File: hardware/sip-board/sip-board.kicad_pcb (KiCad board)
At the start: 8 copper layers, 17 x 50 mm, 85 parts, among them IC1 XC7S15-1CPGA196C, J1 Conn_01x06_Pin, J2 Conn_01x10_Pin, J3 Conn_01x10_Pin, J4 Conn_01x10_Pin, J5 Conn_01x10_Pin, SW1 SW_DIP_x03, SW2 SW_RESET, U1 TLV75718PDRV, U2 TLV75733PDRV, U3 TLV75710PDRV, U4 M95256-WMN6P

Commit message: follow marco stackup
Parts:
- removed C1, C11: 10u, Capacitor_SMD:C_0201_0603Metric
- removed C10, C12, C13, C20, C21, C22, C23, C28, C30, C31, C32, C33, C34, C7, C8, C9: 0.47u, Capacitor_SMD:C_0201_0603Metric
- removed C14, C15, C25, C35, C5: 100u, Capacitor_SMD:C_0201_0603Metric
- removed C16, C17, C18, C19, C26, C27, C29, C36, C37: 4.7u, Capacitor_SMD:C_0201_0603Metric
- removed C2, C3: 50u, Capacitor_SMD:C_0201_0603Metric
- removed C24: 47u, Capacitor_SMD:C_0201_0603Metric
- removed C4, C6: 1u, Capacitor_SMD:C_0201_0603Metric
- removed D1: D_Small, Diode_SMD:D_0201_0603Metric
- removed D2, D3, D4, D5, D6: LED, LED_SMD:LED_0201_0603Metric
- removed IC1: XC7S15-1CPGA196C, fpga_stuff:BGA196C50P14X14_800X800X110
- removed J1: Conn_01x06_Pin, Connector_PinHeader_2.54mm:PinHeader_1x06_P2.54mm_Vertical_SMD_Pin1Right
- removed R1, R2, R3: 1k, Resistor_SMD:R_0201_0603Metric
- removed R10, R11, R12, R13, R4, R5, R6, R7, R8, R9: 10k, Resistor_SMD:R_0201_0603Metric
- removed R14: 5k, Resistor_SMD:R_0201_0603Metric
- removed R15: 2k4, Resistor_SMD:R_0201_0603Metric
- removed R16: 4k7, Resistor_SMD:R_0201_0603Metric
- removed R17, R20: 5k7, Resistor_SMD:R_0201_0603Metric
- removed R18: 2k3, Resistor_SMD:R_0201_0603Metric
- removed R19: 3k, Resistor_SMD:R_0201_0603Metric
- removed SW1: SW_DIP_x03, Button_Switch_SMD:SW_DIP_SPSTx03_Slide_6.7x9.18mm_W6.73mm_P2.54mm_LowProfile_JPin
- removed SW2: SW_RESET, Button_Switch_SMD:SW_Push_1P1T_NO_6x6mm_H9.5mm
- removed U1: TLV75718PDRV, Package_SON:WSON-6-1EP_2x2mm_P0.65mm_EP1x1.6mm
- removed U10, U11, U12, U13, U14, U5, U6, U7, U8, U9: ~, hardware:NXB0104_XQFN12
- removed U2: TLV75733PDRV, Package_SON:WSON-6-1EP_2x2mm_P0.65mm_EP1x1.6mm
- removed U3: TLV75710PDRV, Package_SON:WSON-6-1EP_2x2mm_P0.65mm_EP1x1.6mm
- removed U4: M95256-WMN6P, Package_SO:SOIC-8_3.9x4.9mm_P1.27mm
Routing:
- net +5V: track 132.3 -> 0.00 mm, vias 12 -> 0
- net MOSI: track 65.3 -> 0.00 mm, vias 6 -> 0
- net +3V3: track 64.7 -> 0.00 mm, vias 41 -> 0
- net GND: track 58.4 -> 0.00 mm, vias 58 -> 0
- net CS: track 46.4 -> 0.00 mm, vias 3 -> 0
- net CCLK: track 23.3 -> 0.00 mm, vias 3 -> 0
- net TDO: track 20.8 -> 0.00 mm, vias 3 -> 0
- net +1V8: track 15.1 -> 0.00 mm, vias 4 -> 0
- net M2_CONFIG: track 13.7 -> 0.00 mm, vias 2 -> 0
- net M1_CONFIG: track 13.0 -> 0.00 mm, vias 2 -> 0
- net M0_CONFIG: track 12.7 -> 0.00 mm, vias 2 -> 0
- net PROGRAM_B: track 11.2 -> 0.00 mm
- net DIN: track 11.0 -> 0.00 mm, vias 2 -> 0
- net +1V0: track 10.5 -> 0.00 mm, vias 13 -> 0
- net Net-(C11-Pad1): track 9.44 -> 0.00 mm
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- added copper zone on In6.Cu, net GND
- removed copper zone on In3.Cu, net +1V0
- removed copper zone on In2.Cu, net +3V3
- removed copper zone on B.Cu, net GND
- removed copper zone on In4.Cu, net GND
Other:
- board text removed: "+5V"
- board text removed: "1V0"
- board text removed: "1V8"
- board text removed: "3V3"
- board text removed: "A0"
- board text removed: "A1"
- board text removed: "A10"
- board text removed: "A11"
- board text removed: "A12"
- board text removed: "A13"
- board text removed: "A14"
- board text removed: "A15"
- board text removed: "A2"
- board text removed: "A3"
- board text removed: "A4"
- board text removed: "A5"
- board text removed: "A6"
- board text removed: "A7"
- board text removed: "A8"
- board text removed: "A9"
- board text removed: "BUSAK"
- board text removed: "BUSRQ"
- board text removed: "CLK"
- board text removed: "D0"
- board text removed: "D1"
- board text removed: "D2"
- board text removed: "D3"
- board text removed: "D4"
- board text removed: "D5"
- board text removed: "D6"
- board text removed: "D7"
- board text removed: "GND"
- board text removed: "HALT"
- board text removed: "INT"
- board text removed: "IORQ"
- board text removed: "M0"
- board text removed: "M1"
- board text removed: "M2"
- board text removed: "MREQ"
- board text removed: "NMI"
- board text removed: "RD"
- board text removed: "RESET"
- board text removed: "RFSH"
- board text removed: "SPI - [001] JTAG - [101]"
- board text removed: "SPI PROM"
- board text removed: "VDD GND CCLK TDO MOSI CS"
- board text removed: "WAIT"
- board text removed: "WR"
- board text removed: "Z80 Drop In Connor Leu UT Austin '25"
- board text removed: "off/on"

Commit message: wip layout, part placement
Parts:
- added C1: 10u, Capacitor_SMD:C_0201_0603Metric, F.Cu at (141.7, 94.3)
- added C10: 0.47u, Capacitor_SMD:C_0201_0603Metric, B.Cu at (147.2, 105.8)
- added C11: 10u, Capacitor_SMD:C_0201_0603Metric, F.Cu at (150.9, 116.4)
- added C12: 0.47u, Capacitor_SMD:C_0201_0603Metric, B.Cu at (144.0, 102.2)
- added C13: 0.47u, Capacitor_SMD:C_0201_0603Metric, B.Cu at (147.2, 106.7)
- added C14: 100u, Capacitor_SMD:C_0201_0603Metric, F.Cu at (141.8, 108.8)
- added C15: 100u, Capacitor_SMD:C_0201_0603Metric, F.Cu at (144.9, 108.9)
- added C16: 4.7u, Capacitor_SMD:C_0201_0603Metric, F.Cu at (101.4, 62.9)
- added C17: 4.7u, Capacitor_SMD:C_0201_0603Metric, F.Cu at (147.9, 108.8)
- added C18: 4.7u, Capacitor_SMD:C_0201_0603Metric, F.Cu at (149.8, 108.8)
- added C19: 4.7u, Capacitor_SMD:C_0201_0603Metric, F.Cu at (148.9, 108.8)
- added C2: 50u, Capacitor_SMD:C_0201_0603Metric, F.Cu at (145.6, 94.3)
- added C20: 0.47u, Capacitor_SMD:C_0201_0603Metric, B.Cu at (145.6, 103.8)
- added C21: 0.47u, Capacitor_SMD:C_0201_0603Metric, B.Cu at (144.0, 103.8)
- added C22: 0.47u, Capacitor_SMD:C_0201_0603Metric, B.Cu at (143.6, 103.0)
- added C23: 0.47u, Capacitor_SMD:C_0201_0603Metric, B.Cu at (144.0, 104.6)
- added C24: 47u, Capacitor_SMD:C_0201_0603Metric, F.Cu at (142.9, 108.8)
- added C25: 100u, Capacitor_SMD:C_0201_0603Metric, F.Cu at (145.9, 108.9)
- added C26: 4.7u, Capacitor_SMD:C_0201_0603Metric, F.Cu at (143.9, 108.8)
- added C27: 4.7u, Capacitor_SMD:C_0201_0603Metric, F.Cu at (150.7, 107.0)
- added C28: 0.47u, Capacitor_SMD:C_0201_0603Metric, B.Cu at (146.2, 101.3)
- added C29: 4.7u, Capacitor_SMD:C_0201_0603Metric, F.Cu at (150.7, 105.9)
- added C3: 50u, Capacitor_SMD:C_0201_0603Metric, F.Cu at (149.3, 94.3)
- added C30: 0.47u, Capacitor_SMD:C_0201_0603Metric, B.Cu at (146.2, 102.2)
- added C31: 0.47u, Capacitor_SMD:C_0201_0603Metric, B.Cu at (144.2, 105.8)
- added C32: 0.47u, Capacitor_SMD:C_0201_0603Metric, B.Cu at (144.1, 106.7)
- added C33: 0.47u, Capacitor_SMD:C_0201_0603Metric, F.Cu at (140.5, 107.0)
- added C34: 0.47u, Capacitor_SMD:C_0201_0603Metric, F.Cu at (140.5, 106.0)
- added C35: 100u, Capacitor_SMD:C_0201_0603Metric, F.Cu at (146.9, 108.9)
- added C36: 4.7u, Capacitor_SMD:C_0201_0603Metric, F.Cu at (150.7, 104.8)
- added C37: 4.7u, Capacitor_SMD:C_0201_0603Metric, F.Cu at (150.7, 103.6)
- added C4: 1u, Capacitor_SMD:C_0201_0603Metric, F.Cu at (146.2, 98.3)
- added C5: 100u, Capacitor_SMD:C_0201_0603Metric, F.Cu at (149.9, 98.3)
- added C6: 1u, Capacitor_SMD:C_0201_0603Metric, F.Cu at (142.3, 98.3)
- added C7: 0.47u, Capacitor_SMD:C_0201_0603Metric, B.Cu at (145.7, 106.7)
- added C8: 0.47u, Capacitor_SMD:C_0201_0603Metric, B.Cu at (145.7, 105.8)
- added C9: 0.47u, Capacitor_SMD:C_0201_0603Metric, B.Cu at (144.0, 101.3)
- added CFG1: SW_DIP_x03, Button_Switch_SMD:SW_DIP_SPSTx03_Slide_6.7x9.18mm_W6.73mm_P2.54mm_LowProfile_JPin, F.Cu at (145.4, 123.5)
- added D1: D_Small, Diode_SMD:D_0201_0603Metric, F.Cu at (151.8, 85.7)
- added D3: LED, LED_SMD:LED_0201_0603Metric, F.Cu at (139.9, 97.1)
- added D4: LED, LED_SMD:LED_0201_0603Metric, F.Cu at (143.8, 97.1)
- added D5: LED, LED_SMD:LED_0201_0603Metric, F.Cu at (147.5, 97.1)
- added DONE1: LED, LED_SMD:LED_0201_0603Metric, F.Cu at (145.7, 110.6)
- added IC1: XC7S15-1CPGA196C, fpga_stuff:BGA196C50P14X14_800X800X110, F.Cu at (145.6, 103.3)
- added INIT1: LED, LED_SMD:LED_0201_0603Metric, F.Cu at (142.6, 110.7)
- added J1: Conn_01x06_Pin, Connector_PinHeader_2.54mm:PinHeader_1x06_P2.54mm_Vertical_SMD_Pin1Left, F.Cu at (145.6, 83.3)
- added R1: 1k, Resistor_SMD:R_0201_0603Metric, F.Cu at (149.0, 118.3)
- added R10: 10k, Resistor_SMD:R_0201_0603Metric, F.Cu at (108.8, 64.6)
- added R11: 10k, Resistor_SMD:R_0201_0603Metric, F.Cu at (108.8, 66.4)
- added R12: 10k, Resistor_SMD:R_0201_0603Metric, F.Cu at (108.8, 68.1)
- added R13: 10k, Resistor_SMD:R_0201_0603Metric, F.Cu at (108.8, 69.9)
- added R14: 5k, Resistor_SMD:R_0201_0603Metric, F.Cu at (149.2, 110.7)
- added R15: 2k4, Resistor_SMD:R_0201_0603Metric, F.Cu at (111.2, 55.9)
- added R16: 4k7, Resistor_SMD:R_0201_0603Metric, F.Cu at (144.1, 110.7)
- added R17: 5k7, Resistor_SMD:R_0201_0603Metric, F.Cu at (147.2, 110.6)
- added R18: 2k3, Resistor_SMD:R_0201_0603Metric, F.Cu at (140.7, 98.3)
- added R19: 3k, Resistor_SMD:R_0201_0603Metric, F.Cu at (144.6, 98.3)
- added R2: 1k, Resistor_SMD:R_0201_0603Metric, F.Cu at (146.2, 118.3)
- added R20: 5k7, Resistor_SMD:R_0201_0603Metric, F.Cu at (148.3, 98.3)
- added R3: 1k, Resistor_SMD:R_0201_0603Metric, F.Cu at (143.6, 118.3)
- added R4: 10k, Resistor_SMD:R_0201_0603Metric, F.Cu at (108.8, 54.1)
- added R5: 10k, Resistor_SMD:R_0201_0603Metric, F.Cu at (108.8, 55.9)
- added R6: 10k, Resistor_SMD:R_0201_0603Metric, F.Cu at (108.8, 57.6)
- added R7: 10k, Resistor_SMD:R_0201_0603Metric, F.Cu at (108.8, 59.4)
- added R8: 10k, Resistor_SMD:R_0201_0603Metric, F.Cu at (108.8, 61.1)
- added R9: 10k, Resistor_SMD:R_0201_0603Metric, F.Cu at (108.8, 62.9)
- added SPIPROM1: M95256-WMN6P, Package_SO:SOIC-8_3.9x4.9mm_P1.27mm, F.Cu at (145.4, 89.6)
- added SW2: SW_RESET, Button_Switch_SMD:SW_Push_1P1T_NO_6x6mm_H9.5mm, F.Cu at (145.5, 114.5)
- added U1: TLV75718PDRV, Package_SON:WSON-6-1EP_2x2mm_P0.65mm_EP1x1.6mm, F.Cu at (145.6, 96.5)
- added U10: ~, hardware:NXB0104_XQFN12, F.Cu at (99.7, 52.5)
- added U11: ~, hardware:NXB0104_XQFN12, F.Cu at (102.8, 52.5)
- added U12: ~, hardware:NXB0104_XQFN12, F.Cu at (105.9, 52.5)
- added U13: ~, hardware:NXB0104_XQFN12, F.Cu at (109.0, 52.5)
- added U14: ~, hardware:NXB0104_XQFN12, F.Cu at (112.0, 52.5)
- added U2: TLV75733PDRV, Package_SON:WSON-6-1EP_2x2mm_P0.65mm_EP1x1.6mm, F.Cu at (149.3, 96.5)
- added U3: TLV75710PDRV, Package_SON:WSON-6-1EP_2x2mm_P0.65mm_EP1x1.6mm, F.Cu at (141.7, 96.5)
- added U5: ~, hardware:NXB0104_XQFN12, F.Cu at (131.9, 81.5)
- added U6: ~, hardware:NXB0104_XQFN12, F.Cu at (102.8, 48.5)
- added U7: ~, hardware:NXB0104_XQFN12, F.Cu at (105.9, 48.5)
- added U8: ~, hardware:NXB0104_XQFN12, F.Cu at (109.0, 48.5)
- added U9: ~, hardware:NXB0104_XQFN12, F.Cu at (112.0, 48.5)
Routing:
- net GND: track 0.00 -> 59.5 mm, vias 0 -> 67
- net +3V3: track 0.00 -> 35.1 mm, vias 0 -> 16
- net +5V: track 0.00 -> 29.4 mm
- net CS: track 0.00 -> 21.7 mm
- net +1V8: track 0.00 -> 12.5 mm, vias 0 -> 5
- net CCLK: track 0.00 -> 10.4 mm, vias 0 -> 2
- net +1V0: track 0.00 -> 9.76 mm, vias 0 -> 11
- net PROGRAM_B: track 0.00 -> 9.46 mm
- net Net-(C11-Pad1): track 0.00 -> 9.41 mm
- net MOSI: track 0.00 -> 6.57 mm, vias 0 -> 2
- net DONE: track 0.00 -> 5.55 mm, vias 0 -> 2
- net Net-(IC1-INIT_B_0): track 0.00 -> 4.91 mm, vias 0 -> 2
- net VDD: track 0.00 -> 3.86 mm
- net Net-(D4-A): track 0.00 -> 1.12 mm
- net Net-(D5-A): track 0.00 -> 1.08 mm
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- added copper zone on In4.Cu, net +1V0
- added copper zone on In3.Cu, net +3V3
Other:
- board text added: "CCLK"
- board text added: "CS"
- board text added: "File off bottom of THT connectors"
- board text added: "GND"
- board text added: "MOSI"
- board text added: "TDO"
- board text added: "VDD"

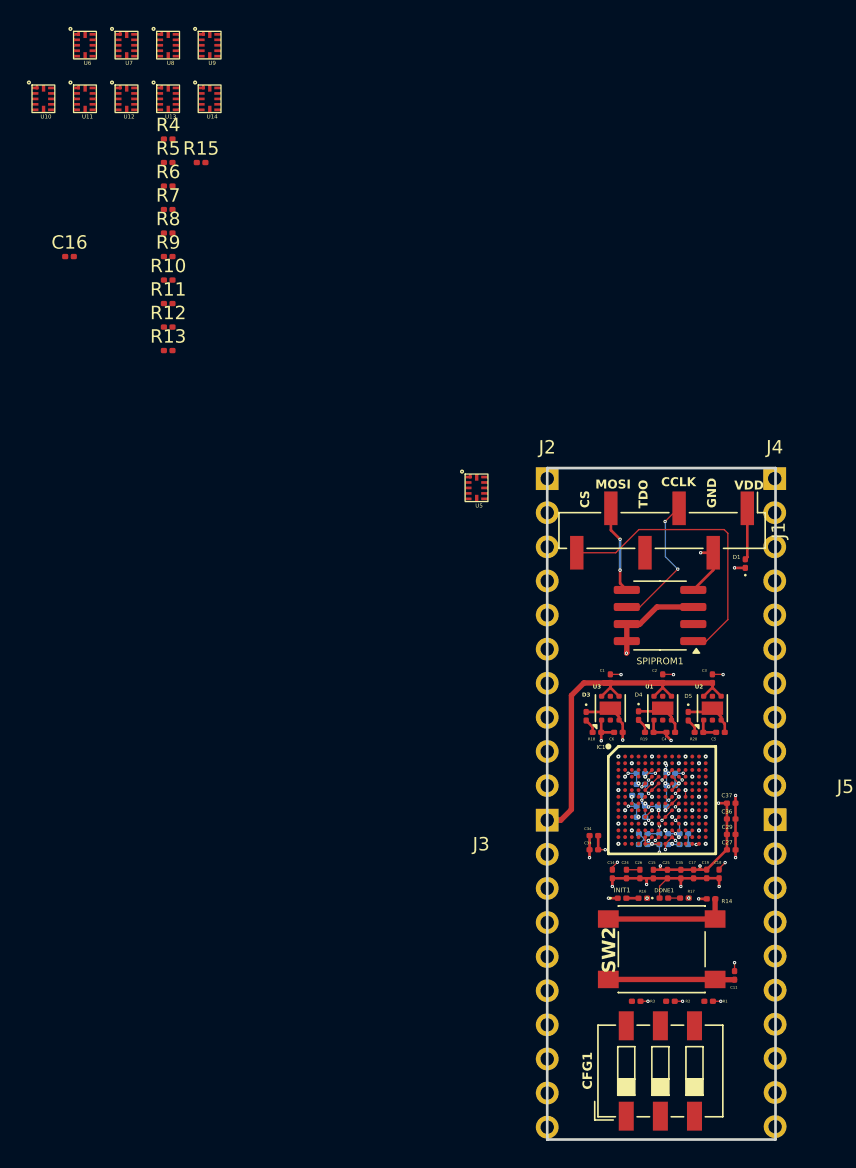
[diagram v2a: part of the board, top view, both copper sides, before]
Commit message: Finish draft 1(.5?) of SiP board. Needs to be looked at again and probably redone.
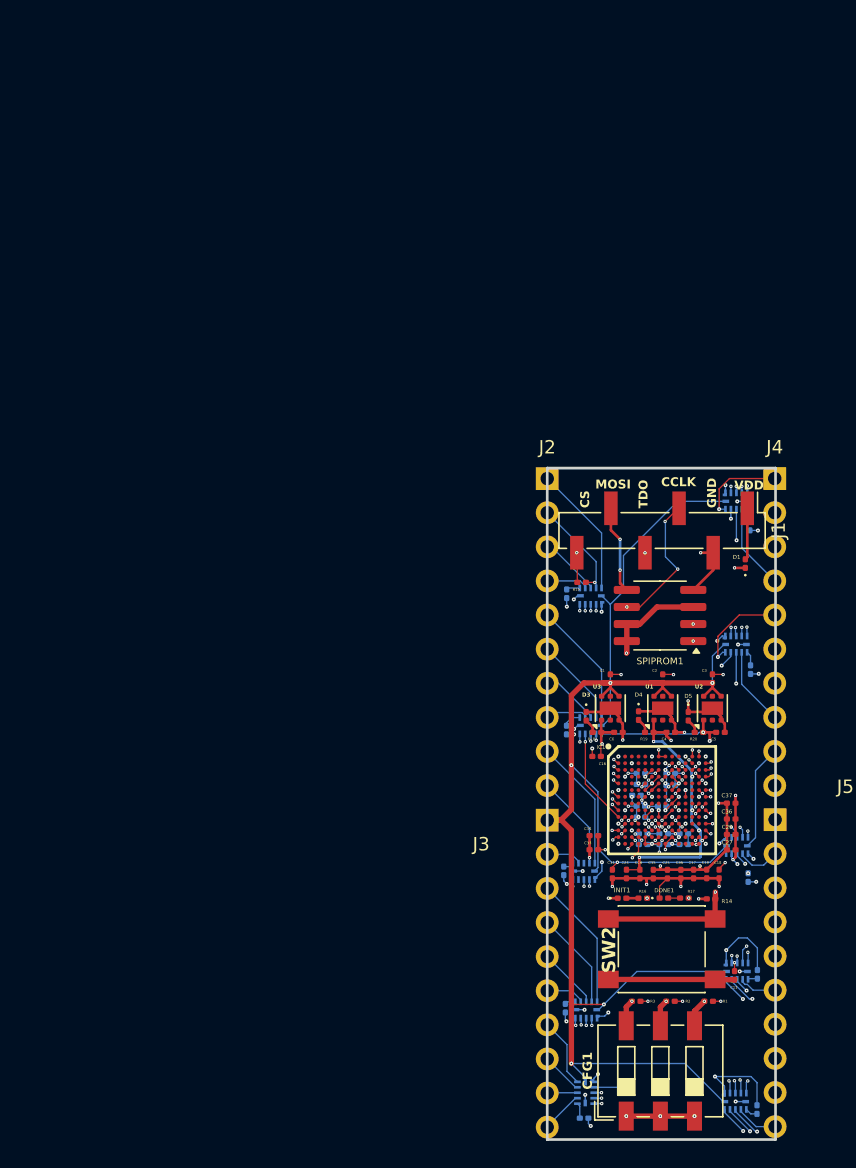
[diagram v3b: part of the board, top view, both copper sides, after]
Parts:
- R10, R11, R12, R13, R4, R5, R6, R7, R8, R9, U10, U11, U12, U13, U14, U5, U6, U7, U8, U9: moved to B.Cu
- moved U14 83.8 mm to (152.4, 126.0), turned to -90 degrees
- moved U9 82.7 mm to (139.7, 126.5), turned to 180 degrees
- moved U13 77.2 mm to (152.5, 116.3), turned to -90 degrees
- moved U8 76.2 mm to (138.5, 118.8), turned to 90 degrees
- moved R8 72.8 mm to (139.7, 127.0), turned to 180 degrees
- moved U12 71.7 mm to (152.5, 106.9), turned to -90 degrees
- moved R13 71.5 mm to (152.6, 126.4), turned to -90 degrees
- moved U7 68.2 mm to (138.4, 108.4), turned to 90 degrees
- moved R7 66.4 mm to (138.3, 118.8), turned to 90 degrees
- moved R12 65.2 mm to (152.7, 116.3), turned to -90 degrees
- moved U11 63.4 mm to (152.4, 91.9), turned to -90 degrees
- moved U6 60.9 mm to (138.9, 97.6), turned to 90 degrees
- moved R11 60.8 mm to (152.0, 109.1), turned to 90 degrees
- moved U10 60.1 mm to (152.5, 81.3), turned to -90 degrees
- moved R6 58.9 mm to (138.2, 108.6), turned to 90 degrees
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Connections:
- IC1 pad A12: unconnected-(IC1-IO_L2N_T0_D03_14-PadA12) -> RD_FPGA
- IC1 pad A13: unconnected-(IC1-IO_0_14-PadA13) -> WAIT_FPGA
- IC1 pad B1: unconnected-(IC1-IO_L5N_T0_34-PadB1) -> A11_FPGA
- IC1 pad B12: unconnected-(IC1-IO_L5N_T0_D07_14-PadB12) -> WR_FPGA
- IC1 pad B14: unconnected-(IC1-IO_L7N_T1_D10_14-PadB14) -> BUSRQ_FPGA
- IC1 pad C1: unconnected-(IC1-IO_L7N_T1_34-PadC1) -> A12_FPGA
- IC1 pad C12: unconnected-(IC1-IO_L5P_T0_D06_14-PadC12) -> BUSAK_FPGA
- IC1 pad C14: unconnected-(IC1-IO_L7P_T1_D09_14-PadC14) -> RESET_FPGA
- IC1 pad D1: unconnected-(IC1-IO_L9N_T1_DQS_34-PadD1) -> A13_FPGA
- IC1 pad D14: unconnected-(IC1-IO_L8N_T1_D12_14-PadD14) -> M1_FPGA
- IC1 pad E1: unconnected-(IC1-IO_L9P_T1_DQS_34-PadE1) -> A14_FPGA
- IC1 pad E13: unconnected-(IC1-IO_L8P_T1_D11_14-PadE13) -> RFSH_FPGA
- IC1 pad F13: unconnected-(IC1-IO_L11N_T1_SRCC_14-PadF13) -> A0_FPGA
- IC1 pad F14: unconnected-(IC1-IO_L12N_T1_MRCC_14-PadF14) -> A1_FPGA
- IC1 pad G1: unconnected-(IC1-IO_L12N_T1_MRCC_34-PadG1) -> A15_FPGA
- IC1 pad G14: unconnected-(IC1-IO_L12P_T1_MRCC_14-PadG14) -> A2_FPGA
- IC1 pad H1: unconnected-(IC1-IO_L15N_T2_DQS_34-PadH1) -> CLK
- IC1 pad H13: unconnected-(IC1-IO_L14N_T2_SRCC_14-PadH13) -> A3_FPGA
- IC1 pad H14: unconnected-(IC1-IO_L15N_T2_DQS_DOUT_CSO_B_14-PadH14) -> A4_FPGA
- IC1 pad J1: unconnected-(IC1-IO_L15P_T2_DQS_34-PadJ1) -> D3_FPGA
- IC1 pad J13: unconnected-(IC1-IO_L14P_T2_SRCC_14-PadJ13) -> A5_FPGA
- IC1 pad J14: unconnected-(IC1-IO_L15P_T2_DQS_RDWR_B_14-PadJ14) -> A6_FPGA
- IC1 pad K1: unconnected-(IC1-IO_L17N_T2_34-PadK1) -> D4_FPGA
- IC1 pad K2: unconnected-(IC1-IO_L18N_T2_34-PadK2) -> D7_FPGA
- IC1 pad K3: unconnected-(IC1-IO_L18P_T2_34-PadK3) -> D0_FPGA
- IC1 pad L14: unconnected-(IC1-IO_L17N_T2_D29_14-PadL14) -> A7_FPGA
- IC1 pad L2: unconnected-(IC1-IO_L17P_T2_34-PadL2) -> D1_FPGA
- IC1 pad L4: unconnected-(IC1-IO_L19P_T3_34-PadL4) -> INT_FPGA
- IC1 pad M1: unconnected-(IC1-IO_L20N_T3_34-PadM1) -> D2_FPGA
- IC1 pad M14: unconnected-(IC1-IO_L17P_T2_D30_14-PadM14) -> A8_FPGA
- IC1 pad M2: unconnected-(IC1-IO_L20P_T3_34-PadM2) -> D6_FPGA
- IC1 pad N1: unconnected-(IC1-IO_L21N_T3_DQS_34-PadN1) -> D5_FPGA
- IC1 pad N13: unconnected-(IC1-IO_L20P_T3_D24_14-PadN13) -> A10_FPGA
- IC1 pad N14: unconnected-(IC1-IO_L20N_T3_D23_14-PadN14) -> A9_FPGA
- IC1 pad N3: unconnected-(IC1-IO_L22N_T3_34-PadN3) -> NMI_FPGA
- IC1 pad N4: unconnected-(IC1-IO_L24P_T3_34-PadN4) -> HALT_FPGA
- IC1 pad P3: unconnected-(IC1-IO_L23P_T3_34-PadP3) -> MREQ_FPGA
- IC1 pad P4: unconnected-(IC1-IO_L22P_T3_34-PadP4) -> IORQ_FPGA
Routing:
- net +5V: track 29.4 -> 122.9 mm, vias 0 -> 5
- net +3V3: track 35.1 -> 72.3 mm, vias 16 -> 40
- net WR_FPGA: track 0.00 -> 23.9 mm, vias 0 -> 2
- net TDO: track 0.00 -> 23.5 mm, vias 0 -> 2
- net BUSAK_FPGA: track 0.00 -> 23.1 mm, vias 0 -> 2
- net A7_FPGA: track 0.00 -> 23.0 mm, vias 0 -> 2
- net MOSI: track 6.57 -> 28.7 mm, vias 2 -> 4
- net WAIT_FPGA: track 0.00 -> 22.2 mm, vias 0 -> 2
- net RD_FPGA: track 0.00 -> 21.8 mm, vias 0 -> 2
- net HALT_FPGA: track 0.00 -> 21.6 mm, vias 0 -> 4
- net NMI_FPGA: track 0.00 -> 21.4 mm, vias 0 -> 2
- net IORQ_FPGA: track 0.00 -> 21.1 mm, vias 0 -> 2
- net A10_FPGA: track 0.00 -> 20.8 mm, vias 0 -> 2
- net A8_FPGA: track 0.00 -> 20.6 mm, vias 0 -> 2
- net MREQ_FPGA: track 0.00 -> 20.5 mm, vias 0 -> 2
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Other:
- board text added: "Team: Nadia Houston, April Douglas, Connor Leu, Gage Miller, Luke Mason, Gabriel Moore"
- board text added: "Z80 Drop In By Connor Leu ECE UT Austin '25"

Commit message: add new spi chip supported by vivado
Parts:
- removed C1, C11: 10u, Capacitor_SMD:C_0201_0603Metric
- removed C10, C12, C13, C20, C21, C22, C23, C28, C30, C31, C32, C33, C34, C7, C8, C9: 0.47u, Capacitor_SMD:C_0201_0603Metric
- removed C14, C15, C25, C35, C5: 100u, Capacitor_SMD:C_0201_0603Metric
- removed C16, C17, C18, C19, C26, C27, C29, C36, C37: 4.7u, Capacitor_SMD:C_0201_0603Metric
- removed C2, C3: 50u, Capacitor_SMD:C_0201_0603Metric
- removed C24: 47u, Capacitor_SMD:C_0201_0603Metric
- removed C4, C6: 1u, Capacitor_SMD:C_0201_0603Metric
- removed CFG1: SW_DIP_x03, Button_Switch_SMD:SW_DIP_SPSTx03_Slide_6.7x9.18mm_W6.73mm_P2.54mm_LowProfile_JPin
- removed D1: D_Small, Diode_SMD:D_0201_0603Metric
- removed D3, D4, D5, DONE1, INIT1: LED, LED_SMD:LED_0201_0603Metric
- removed IC1: XC7S15-1CPGA196C, fpga_stuff:BGA196C50P14X14_800X800X110
- removed J1: Conn_01x06_Pin, Connector_PinHeader_2.54mm:PinHeader_1x06_P2.54mm_Vertical_SMD_Pin1Left
- removed J2, J3, J4, J5: Conn_01x10_Pin, Connector_PinHeader_2.54mm:PinHeader_1x10_P2.54mm_Vertical
- removed R1, R2, R3: 1k, Resistor_SMD:R_0201_0603Metric
- removed R10, R11, R12, R13, R4, R5, R6, R7, R8, R9: 10k, Resistor_SMD:R_0201_0603Metric
- removed R14: 5k, Resistor_SMD:R_0201_0603Metric
- removed R15: 2k4, Resistor_SMD:R_0201_0603Metric
- removed R16: 4k7, Resistor_SMD:R_0201_0603Metric
- removed R17, R20: 5k7, Resistor_SMD:R_0201_0603Metric
- removed R18: 2k3, Resistor_SMD:R_0201_0603Metric
- removed R19: 3k, Resistor_SMD:R_0201_0603Metric
- removed SPIPROM1: M95256-WMN6P, Package_SO:SOIC-8_3.9x4.9mm_P1.27mm
- removed SW2: SW_RESET, Button_Switch_SMD:SW_Push_1P1T_NO_6x6mm_H9.5mm
- removed U1: TLV75718PDRV, Package_SON:WSON-6-1EP_2x2mm_P0.65mm_EP1x1.6mm
- removed U10, U11, U12, U13, U14, U5, U6, U7, U8, U9: ~, hardware:NXB0104_XQFN12
- removed U2: TLV75733PDRV, Package_SON:WSON-6-1EP_2x2mm_P0.65mm_EP1x1.6mm
- removed U3: TLV75710PDRV, Package_SON:WSON-6-1EP_2x2mm_P0.65mm_EP1x1.6mm
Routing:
- net +5V: track 122.9 -> 0.00 mm, vias 5 -> 0
- net GND: track 75.6 -> 0.00 mm, vias 79 -> 0
- net +3V3: track 72.3 -> 0.00 mm, vias 40 -> 0
- net CS: track 29.3 -> 0.00 mm, vias 4 -> 0
- net +1V8: track 29.1 -> 0.00 mm, vias 7 -> 0
- net MOSI: track 28.7 -> 0.00 mm, vias 4 -> 0
- net WR_FPGA: track 23.9 -> 0.00 mm, vias 2 -> 0
- net TDO: track 23.5 -> 0.00 mm, vias 2 -> 0
- net BUSAK_FPGA: track 23.1 -> 0.00 mm, vias 2 -> 0
- net A7_FPGA: track 23.0 -> 0.00 mm, vias 2 -> 0
- net CCLK: track 23.0 -> 0.00 mm, vias 4 -> 0
- net WAIT_FPGA: track 22.2 -> 0.00 mm, vias 2 -> 0
- net RD_FPGA: track 21.8 -> 0.00 mm, vias 2 -> 0
- net HALT_FPGA: track 21.6 -> 0.00 mm, vias 4 -> 0
- net NMI_FPGA: track 21.4 -> 0.00 mm, vias 2 -> 0
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- removed copper zone on In4.Cu, net +1V0
- removed copper zone on In3.Cu, net +3V3
- removed copper zone on In1.Cu, net GND
- removed copper zone on In6.Cu, net GND
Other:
- board outline removed
- board text removed: "CCLK"
- board text removed: "CS"
- board text removed: "File off bottom of THT connectors"
- board text removed: "GND"
- board text removed: "MOSI"
- board text removed: "TDO"
- board text removed: "Team: Nadia Houston, April Douglas, Connor Leu, Gage Miller, Luke Mason, Gabriel Moore"
- board text removed: "VDD"
- board text removed: "Z80 Drop In By Connor Leu ECE UT Austin '25"
